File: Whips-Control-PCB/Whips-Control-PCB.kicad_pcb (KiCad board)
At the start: 2 copper layers, 72.5 x 72.5 mm, 6 parts, among them J1 PWR, J2 DATA, U1 Teensy4.1_Minimal, U2 MAX485E, U3 TSOP341xx

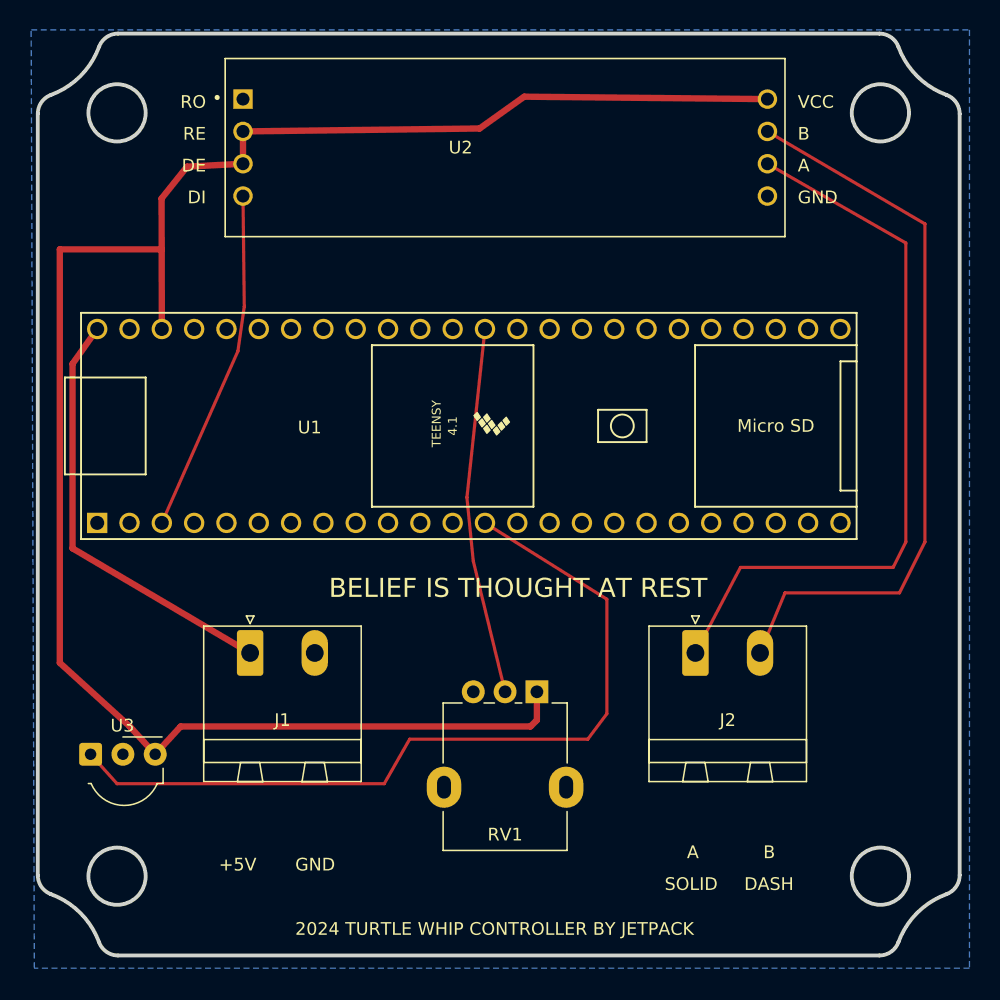
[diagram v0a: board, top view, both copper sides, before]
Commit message: this is a new PCB for the controller, to fit in a smaller box
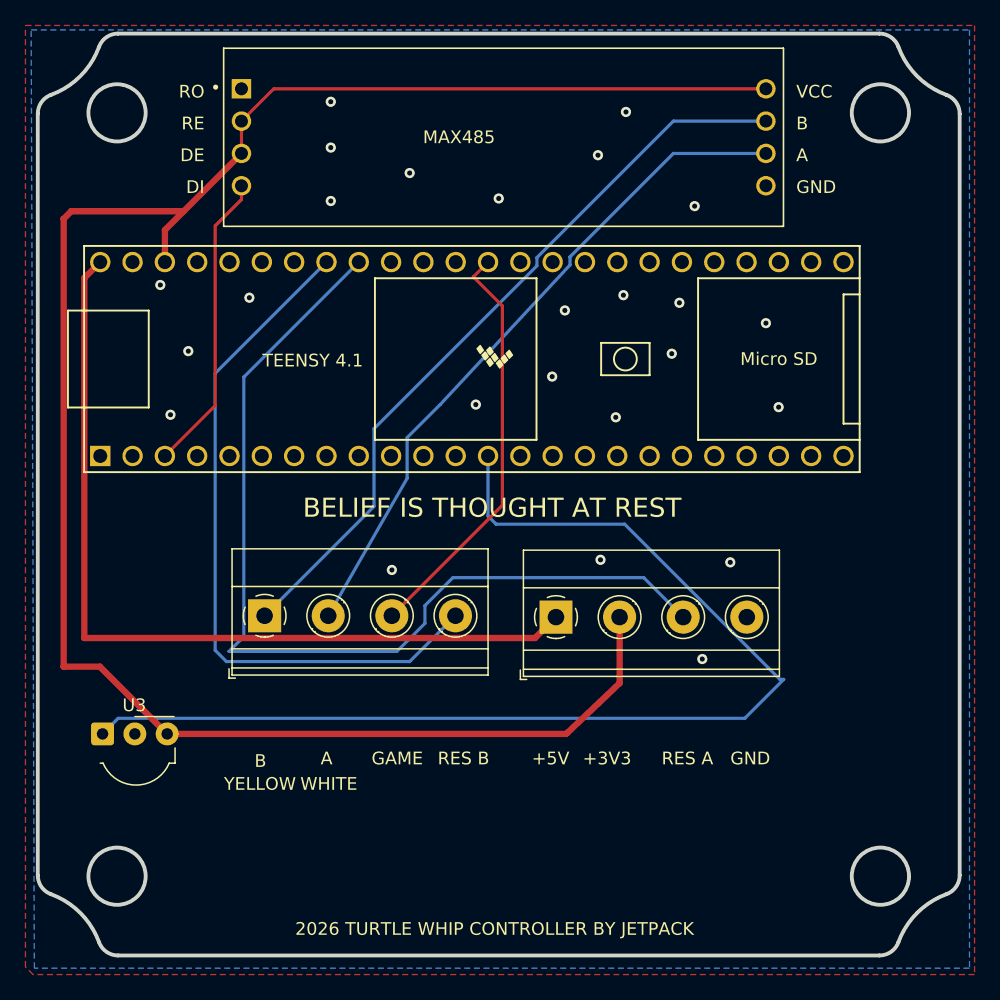
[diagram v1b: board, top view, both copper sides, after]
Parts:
- removed J2: DATA, Connector_Phoenix_MSTB:PhoenixContact_MSTBA_2,5_2-G-5,08_1x02_P5.08mm_Horizontal
- removed RV1: R_Potentiometer_US, Potentiometer_THT:Potentiometer_Alpha_RD901F-40-00D_Single_Vertical
- added J4: Conn_01x04_Pin, TerminalBlock_Phoenix:TerminalBlock_Phoenix_MKDS-1,5-4_1x04_P5.00mm_Horizontal, F.Cu at (90.6, 87.8)
- J1: value PWR -> Conn_01x04_Pin; footprint Connector_Phoenix_MSTB:PhoenixContact_MSTBA_2,5_2-G-5,08_1x02_P5.08mm_Horizontal -> TerminalBlock_Phoenix:TerminalBlock_Phoenix_MKDS-1,5-4_1x04_P5.00mm_Horizontal
- TEENSY 4.1: renamed from U1
- moved J1 24.2 mm to (113.5, 87.9)
- moved TEENSY 4.1 5.27 mm to (106.9, 67.6)
- moved U3 1.86 mm to (77.9, 97.1)
- moved MAX485 0.82 mm to (109.4, 50.2)
- renumbered U2 to MAX485
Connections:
- J1 pad 2: GND -> +3.3V
- TEENSY 4.1 pad 36: /BRIGHT -> /GAME
- TEENSY 4.1 pad 40: unconnected-(U1-18_A4_SDA-Pad40) -> /RESERVEDA
- TEENSY 4.1 pad 41: unconnected-(U1-19_A5_SCL-Pad41) -> /RESERVEDB
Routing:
- net /RESERVEDA: track 0.00 -> 75.0 mm
- net /RESERVEDB: track 0.00 -> 54.9 mm
- net +5V: track 34.1 -> 67.8 mm
- net /GAME: track 0.00 -> 32.8 mm
- net /BRIGHT: track 28.9 -> 0.00 mm
- net /IR: track 64.9 -> 88.6 mm
- net +3.3V: track 146.7 -> 153.4 mm
- net /A: track 57.9 -> 53.7 mm
- net /DI: track 27.0 -> 23.7 mm
- net /B: track 57.9 -> 59.5 mm
- net GND: vias 0 -> 25
- added copper zone on F.Cu, net GND
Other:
- board text added: "+3V3"
- board text added: "2026 TURTLE WHIP CONTROLLER BY JETPACK"
- board text added: "GAME"
- board text added: "RES A"
- board text added: "RES B"
- board text added: "WHITE"
- board text added: "YELLOW"
- board text removed: "2024 TURTLE WHIP CONTROLLER BY JETPACK"
- board text removed: "DASH"
- board text removed: "SOLID"
